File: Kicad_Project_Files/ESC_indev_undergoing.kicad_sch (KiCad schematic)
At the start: 64 parts, among them J2 JST_PH_1x04_P2mm, J3 JST_PH_1x04_P2mm, Q1 NMOS, Q2 NMOS, Q3 NMOS, Q4 NMOS, Q5 NMOS, Q6 NMOS, SW1 SW_Push, SW2 SW_Push, U1 TPS560430X3FDBVR, U11 LMV324, U2 IR2110S, U3 IR2110S, U4 IR2110S, U5 ESP32-WROOM-32E

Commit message: major updates
updated GPIO assignments along with some component orientation , also changed the dimensions to fit everything in
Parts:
- added R26, R27, R28: R_US, Resistor_SMD:R_2512_6332Metric_Pad1.40x3.35mm_HandSolder, symbol Device:R_US
- added U15, U16, U17: INA240A1PW, Package_SO:TSSOP-8_4.4x3mm_P0.65mm, symbol Amplifier_Current:INA240A1PW
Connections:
- net +3.3V: now also U15.5 (V+), U15.6 (REF2), U16.5 (V+), U16.6 (REF2), U17.5 (V+), U17.6 (REF2)
- net GND: now also U15.1 (GND), U15.4 (GND), U15.7 (REF1), U16.1 (GND), U16.4 (GND), U16.7 (REF1), U17.1 (GND), U17.4 (GND), U17.7 (REF1)
- net HIN1: now also U5.31 (IO19); no longer U5.10 (IO25)
- net HIN2: now also U5.28 (IO17)
- net HIN3: now also U5.26 (IO4)
- net LIN1: now also U5.30 (IO18)
- net LIN2: now also U5.27 (IO16)
- net LIN3: now also U5.16 (IO13)
- net P1: now also R26.1, U15.2 (+); no longer U6.
- net P2: now also R27.1, U16.2 (+); no longer U7.
- net P3: now also R28.1, U17.2 (+); no longer U8.
- net Bemf1: now reaches U5.8 (IO32)
- net Bemf1: now also U11.1; no longer U11.8
- net at U5.12 (IO27): no longer U11.7
- net at U5.11 (IO26): no longer U11.1
- net Isen1: now reaches U5.4 (SENSOR_VP)
- net Isen1: now also U15.8
- net Isen2: now reaches U5.5 (SENSOR_VN)
- net Isen2: now also U16.8
- net Isen3: now reaches U5.6 (IO34)
- net Isen3: now also U17.8
- net Bemf2: now reaches U5.9 (IO33)
- net Bemf2: now also U11.7
- new net Bemf3: U11.8, U5.10 (IO25)
- new net PR1: R26.2, U15.3 (-), U6.
- new net PR2: R27.2, U16.3 (-), U7.
- new net PR3: R28.2, U17.3 (-), U8.
- no-connect marks 19 -> 7

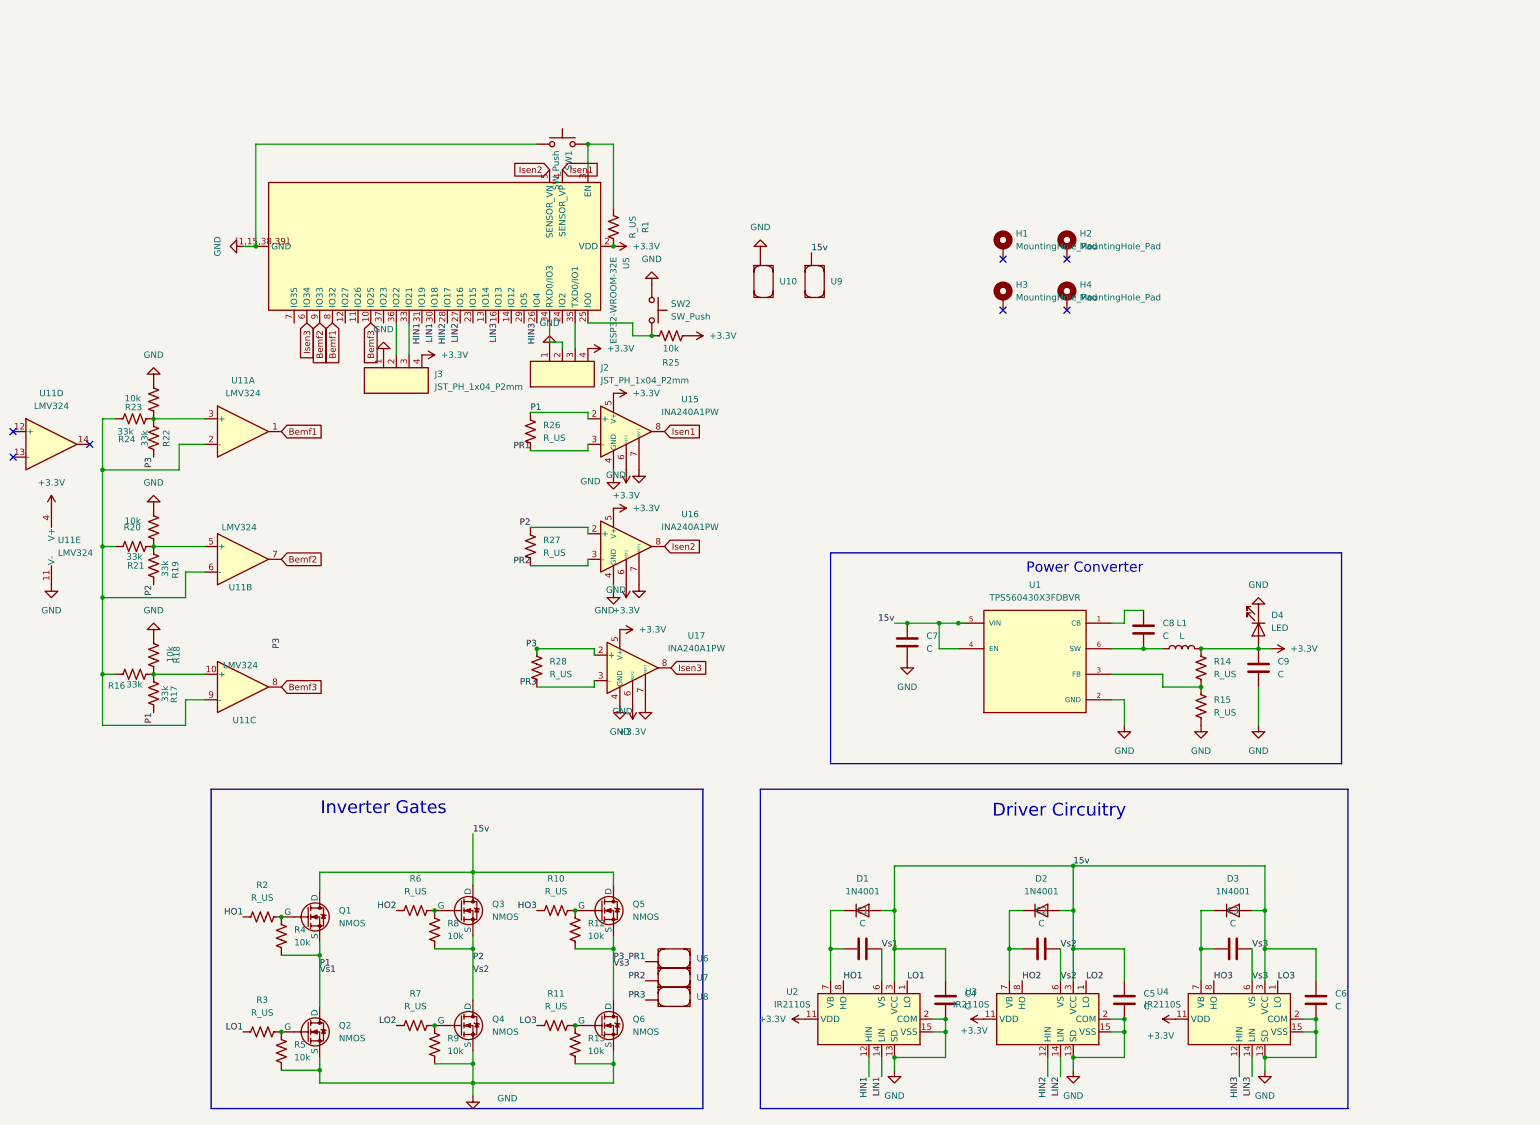
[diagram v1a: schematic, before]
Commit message: updated schematic with comp values
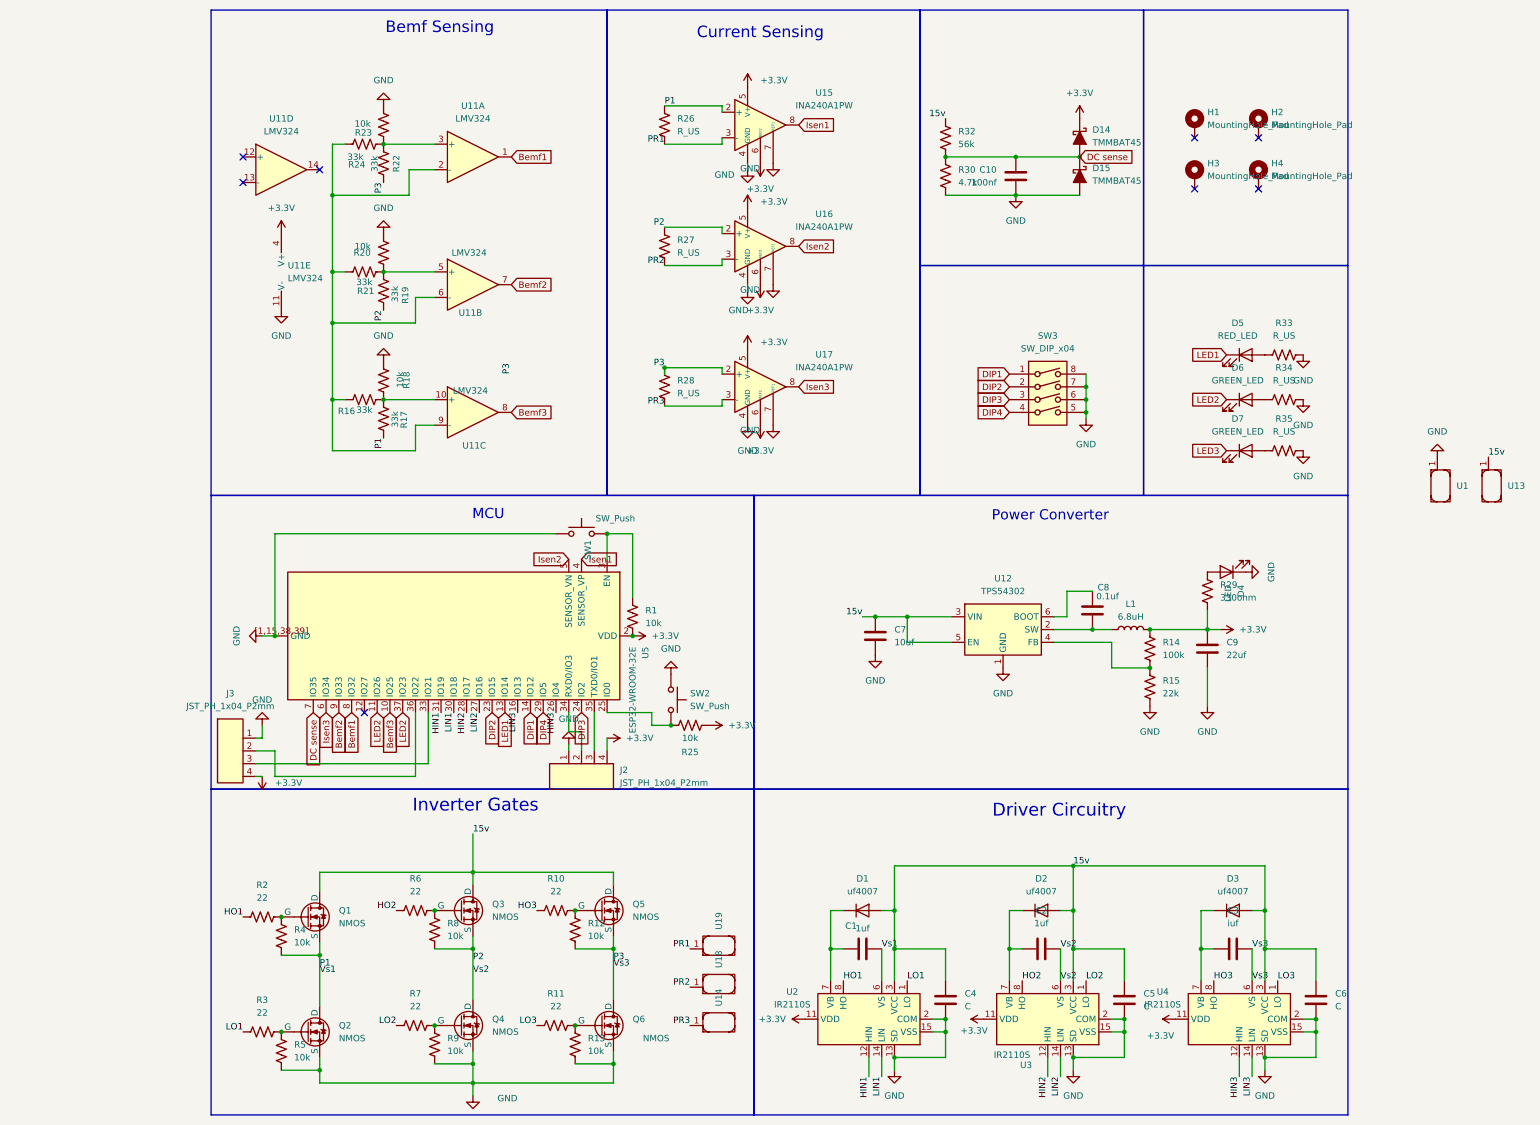
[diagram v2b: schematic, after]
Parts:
- removed U1: TPS560430X3FDBVR, Kicad_Project_Files:IC_TPS560430X3FDBVR, symbol TPS560430X3FDBVR:TPS560430X3FDBVR
- removed U10, U6, U7, U8, U9: (no value), solderpads:Untitled, symbol solderpad_Library:solderpad_1
- added C10: 100nf, Capacitor_SMD:C_0805_2012Metric_Pad1.18x1.45mm_HandSolder, symbol Device:C
- added D14, D15: TMMBAT45, PCM_Diode_SMD_AKL:D_MiniMELF, symbol PCM_Diode_Schottky_AKL:TMMBAT45
- added D5: RED_LED, LED_SMD:LED_1206_3216Metric, symbol Device:LED
- added D6, D7: GREEN_LED, LED_SMD:LED_1206_3216Metric, symbol Device:LED
- added R29: 330ohm, PCM_Resistor_SMD_AKL:R_0805_2012Metric, symbol Device:R_US
- added R30: 4.7k, PCM_Resistor_SMD_AKL:R_0805_2012Metric, symbol Device:R_US
- added R32: 56k, PCM_Resistor_SMD_AKL:R_0805_2012Metric, symbol Device:R_US
- added R33, R34, R35: R_US, PCM_Resistor_SMD_AKL:R_0603_1608Metric_Pad1.05x0.95mm_HandSolder, symbol Device:R_US
- added SW3: SW_DIP_x04, Button_Switch_SMD:SW_DIP_SPSTx04_Slide_6.7x11.72mm_W8.61mm_P2.54mm_LowProfile, symbol Switch:SW_DIP_x04
- added U1, U13, U14, U18, U19: (no value), solderpads:Untitled, symbol solderpad_Library:solderpad_1
- added U12: TPS54302, Package_TO_SOT_SMD:SOT-23-6, symbol Regulator_Switching:TPS54302
- C1, C2: value C -> 1uf
- C3: value C -> iuf
- C7: value C -> 10uf
- C8: value C -> 0.1uf
- C9: value C -> 22uf
- D1, D2, D3: value 1N4001 -> uf4007
- L1: value L -> 6.8uH
- R1: value R_US -> 10k
- R10, R11, R2, R3, R6, R7: value R_US -> 22
- R14: value R_US -> 100k
- R15: value R_US -> 22k
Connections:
- net +3.3V: now also D14.1 (K), R29.2; no longer D4.2 (A)
- net 15v: now also R32.1, U12.3 (VIN), U12.5 (EN), U13.1
- net GND: now also C10.2, D15.2 (A), R30.2, R33.2, R34.2, R35.2, SW3.5, SW3.6, SW3.7, SW3.8, U1.1, U12.1 (GND)
- net PR1: now also U19.1
- net PR2: now also U18.1
- net PR3: now also U14.1
- net at C8.2, L1.1: now also U12.2 (SW)
- net at R14.2, R15.1: now also U12.4 (FB)
- net at C8.1: now also U12.6 (BOOT)
- net LED2: now reaches U5.11 (IO26)
- net LED2: now also U5.37 (IO23), D6.1 (K)
- net LED1: now reaches U5.13 (IO14)
- net LED1: now also D5.1 (K)
- net DIP1: now reaches U5.14 (IO12)
- net DIP1: now also SW3.1
- net DIP2: now reaches U5.23 (IO15)
- net DIP2: now also SW3.2
- net DIP3: now reaches U5.24 (IO2)
- net DIP3: now also SW3.3
- net DIP4: now reaches U5.29 (IO5)
- net DIP4: now also SW3.4
- net DC sense: now reaches U5.7 (IO35)
- net DC sense: now also C10.1, D14.2 (A), D15.1 (K), R30.1, R32.2
- new net: D5.2 (A), R33.1
- new net: D6.2 (A), R34.1
- new net: D4.2 (A), R29.1
- new net: D7.2 (A), R35.1
- new net LED3: D7.1 (K)
- no-connect marks 7 -> 8
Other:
- note added: "Bemf Sensing"
- note added: "Current Sensing"
- note added: "MCU"
- moved on the sheet: C7, C8, C9, D4, H1, H2, H3, H4, J2, J3, L1, R1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
